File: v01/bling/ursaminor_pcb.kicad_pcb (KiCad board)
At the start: 2 copper layers, 298.8 x 122 mm, 233 parts, among them J1 USB_C_Receptacle_USB2.0, J2 I2C-L, J3 I2C-R, J4 AVR-ISP-6, SW1 Reset, U1 ATmega32U4-AU, U2 MCP23017_SO, U3 IS31FL3733-TQ, U4 HOLE, U4 IS31FL3733-TQ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

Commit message: Update footprints
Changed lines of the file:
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@@
   (general
     (thickness 1.6)
-    (drawings 382)
+    (drawings 383)
     (tracks 4358)
     (zones 0)
@@
     (34 B.Paste user hide)
     (35 F.Paste user hide)
-    (36 B.SilkS user hide)
-    (37 F.SilkS user hide)
-    (38 B.Mask user hide)
-    (39 F.Mask user hide)
+    (36 B.SilkS user)
+    (37 F.SilkS user)
+    (38 B.Mask user)
+    (39 F.Mask user)
     (40 Dwgs.User user hide)
     (41 Cmts.User user hide)
@@
     (pad S1 thru_hole oval (at 4.32 1.05 110) (size 1 1.6) (drill oval 0.6 1.2) (layers *.Cu *.Mask)
       (net 1 GND))
-    (model ${KISYS3DMOD}/Connector_USB.3dshapes/USB_C_Receptacle_HRO_TYPE-C-31-M-12.wrl
-      (at (xyz 0 0 0))
+    (model "/home/mark/code/ursaminor/sym/Type-C.pretty/HRO  TYPE-C-31-M-12.step"
+      (offset (xyz -4.5 -3.5 0))
       (scale (xyz 1 1 1))
-      (rotate (xyz 0 0 0))
+      (rotate (xyz -90 0 0))
     )
   )
@@
     (pad S1 thru_hole oval (at 4.32 1.05 180) (size 1 1.6) (drill oval 0.6 1.2) (layers *.Cu *.Mask)
       (net 1 GND))
-    (model ${KISYS3DMOD}/Connector_USB.3dshapes/USB_C_Receptacle_HRO_TYPE-C-31-M-12.wrl
+    (model "${KIPRJMOD}/sym/Type-C.pretty/HRO TYPE-C-31-M-12.step"
       (at (xyz 0 0 0))
       (scale (xyz 1 1 1))
       (rotate (xyz 0 0 0))
     )
+    (model "/home/mark/code/ursaminor/sym/Type-C.pretty/HRO  TYPE-C-31-M-12.step"
+      (offset (xyz -4.5 -3.5 0))
+      (scale (xyz 1 1 1))
+      (rotate (xyz -90 0 0))
+    )
   )
   (module MountingHole:MountingHole_2.2mm_M2_DIN965_Pad (layer F.Cu)
@@
     )
   )
+  (gr_line (start 145.258596 42.35) (end 147.25 42.35) (layer Edge.Cuts) (width 0.05))
   (gr_line (start 181.2044 89.75) (end 179.2232 89.75) (layer Edge.Cuts) (width 0.05))
   (gr_line (start 179.2232 84.65) (end 181.2 84.65) (layer Edge.Cuts) (width 0.05))

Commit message: Fix LED driver wiring
- Caps were not in ordered as per the docs. This doesn't matter *too*
  much but it is nice to be more correct.
- IS31FL3733 needs SDB set high to ensure the chip is always on.
  Previously it was pulled low causing the chip to shut off.
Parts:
- moved C13 3.51 mm to (95.7, 98.7)
- moved C19 3.46 mm to (95.7, 102.0)
- moved C12 2.78 mm to (91.7, 93.3)
- moved C18 2.60 mm to (88.8, 93.3)
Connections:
- R11 pad 1: Net-(R11-Pad1) -> +5V
- R9 pad 1: Net-(R9-Pad1) -> VBUS
- U3 pad 46: Net-(R9-Pad1) -> VBUS
- U4 pad 46: Net-(R11-Pad1) -> +5V
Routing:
- net +5V: track 272.2 -> 305.3 mm, vias 11 -> 13
- net VBUS: track 213.3 -> 226.8 mm, vias 11 -> 12
- net Net-(R9-Pad1): track 4.97 -> 0.00 mm
- net Net-(R11-Pad1): track 4.49 -> 0.00 mm

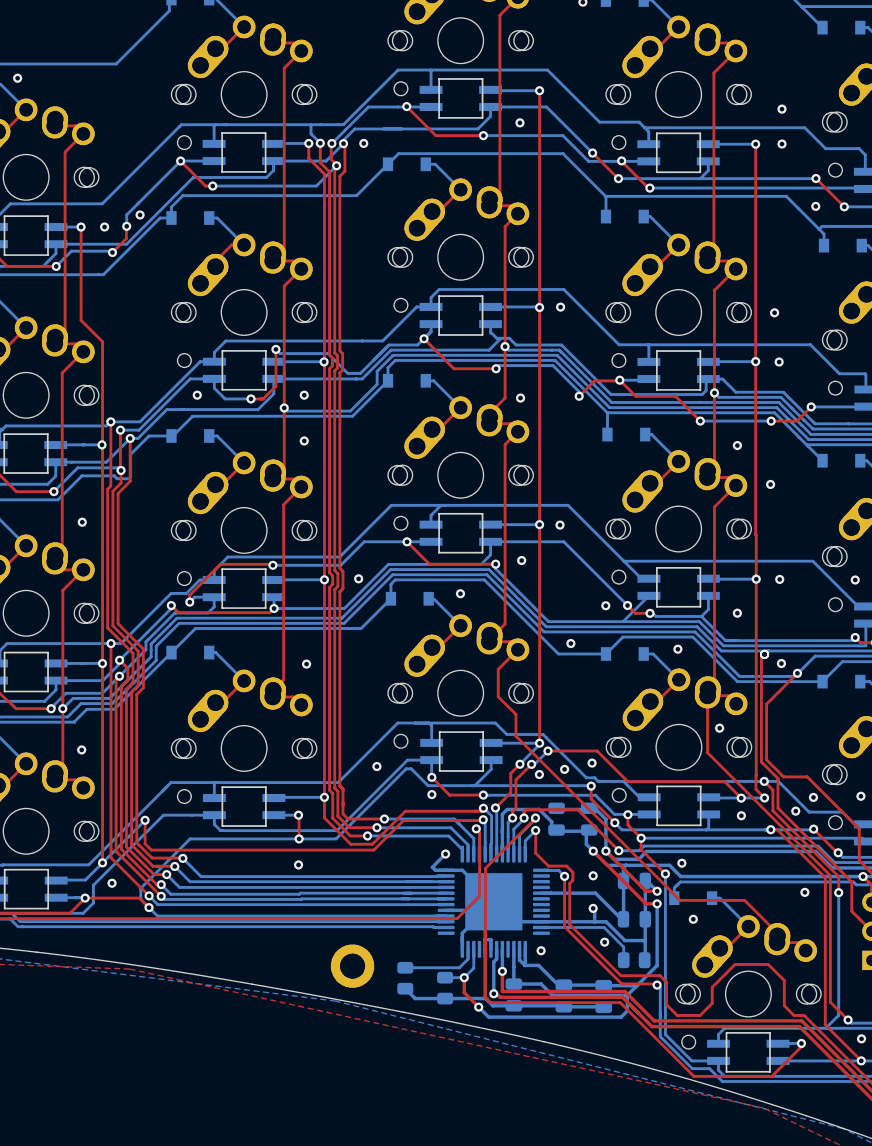
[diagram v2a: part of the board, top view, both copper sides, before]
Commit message: Tweak routing to improve fill areas
Found some gaps on the printed boards that could be filled.
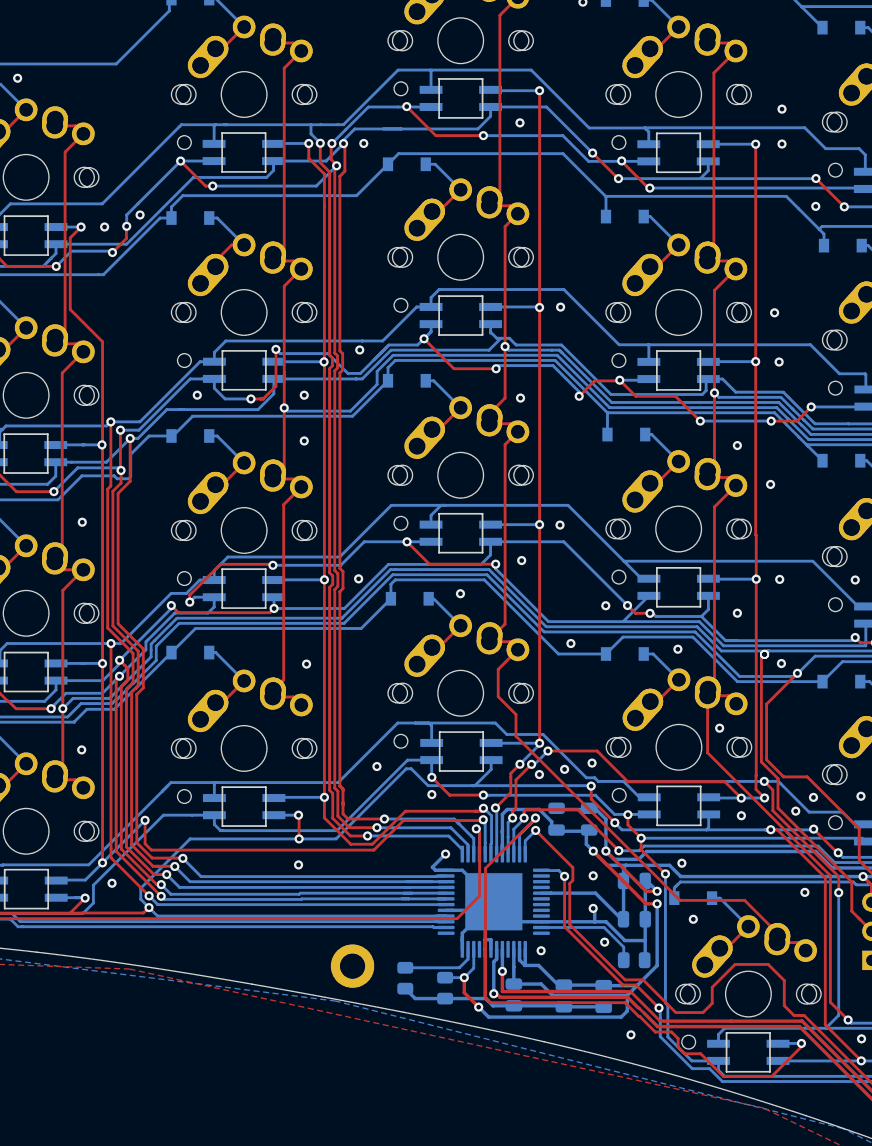
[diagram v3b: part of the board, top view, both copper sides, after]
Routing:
- net Left-CS8: track 69.6 -> 67.3 mm
- net Left-CS9: track 79.6 -> 78.2 mm
- net Left-SW3: track 216.7 -> 217.9 mm
- net SCL-L: track 184.5 -> 183.5 mm
- net Left-CS2: track 114.1 -> 114.9 mm
- net GND: vias 91 -> 93
